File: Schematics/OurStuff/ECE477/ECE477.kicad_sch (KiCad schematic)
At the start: 50 parts, among them J1 USB_B_Micro, J2 Barrel_Jack, J3 OLED JST PH 7pin, J4 Microphone Connector, J5 Conn_01x02_Pin, J6 Conn_01x02_Pin, Q1 SS8050-G, Q2 SS8050-G, SW1 Boot Button, SW2 RST Button, SW3 Button 1, SW4 Button 2, U1 ESP32-WROOM-32E, U2 CP2102N-Axx-xQFN28, U3 D30V30F3

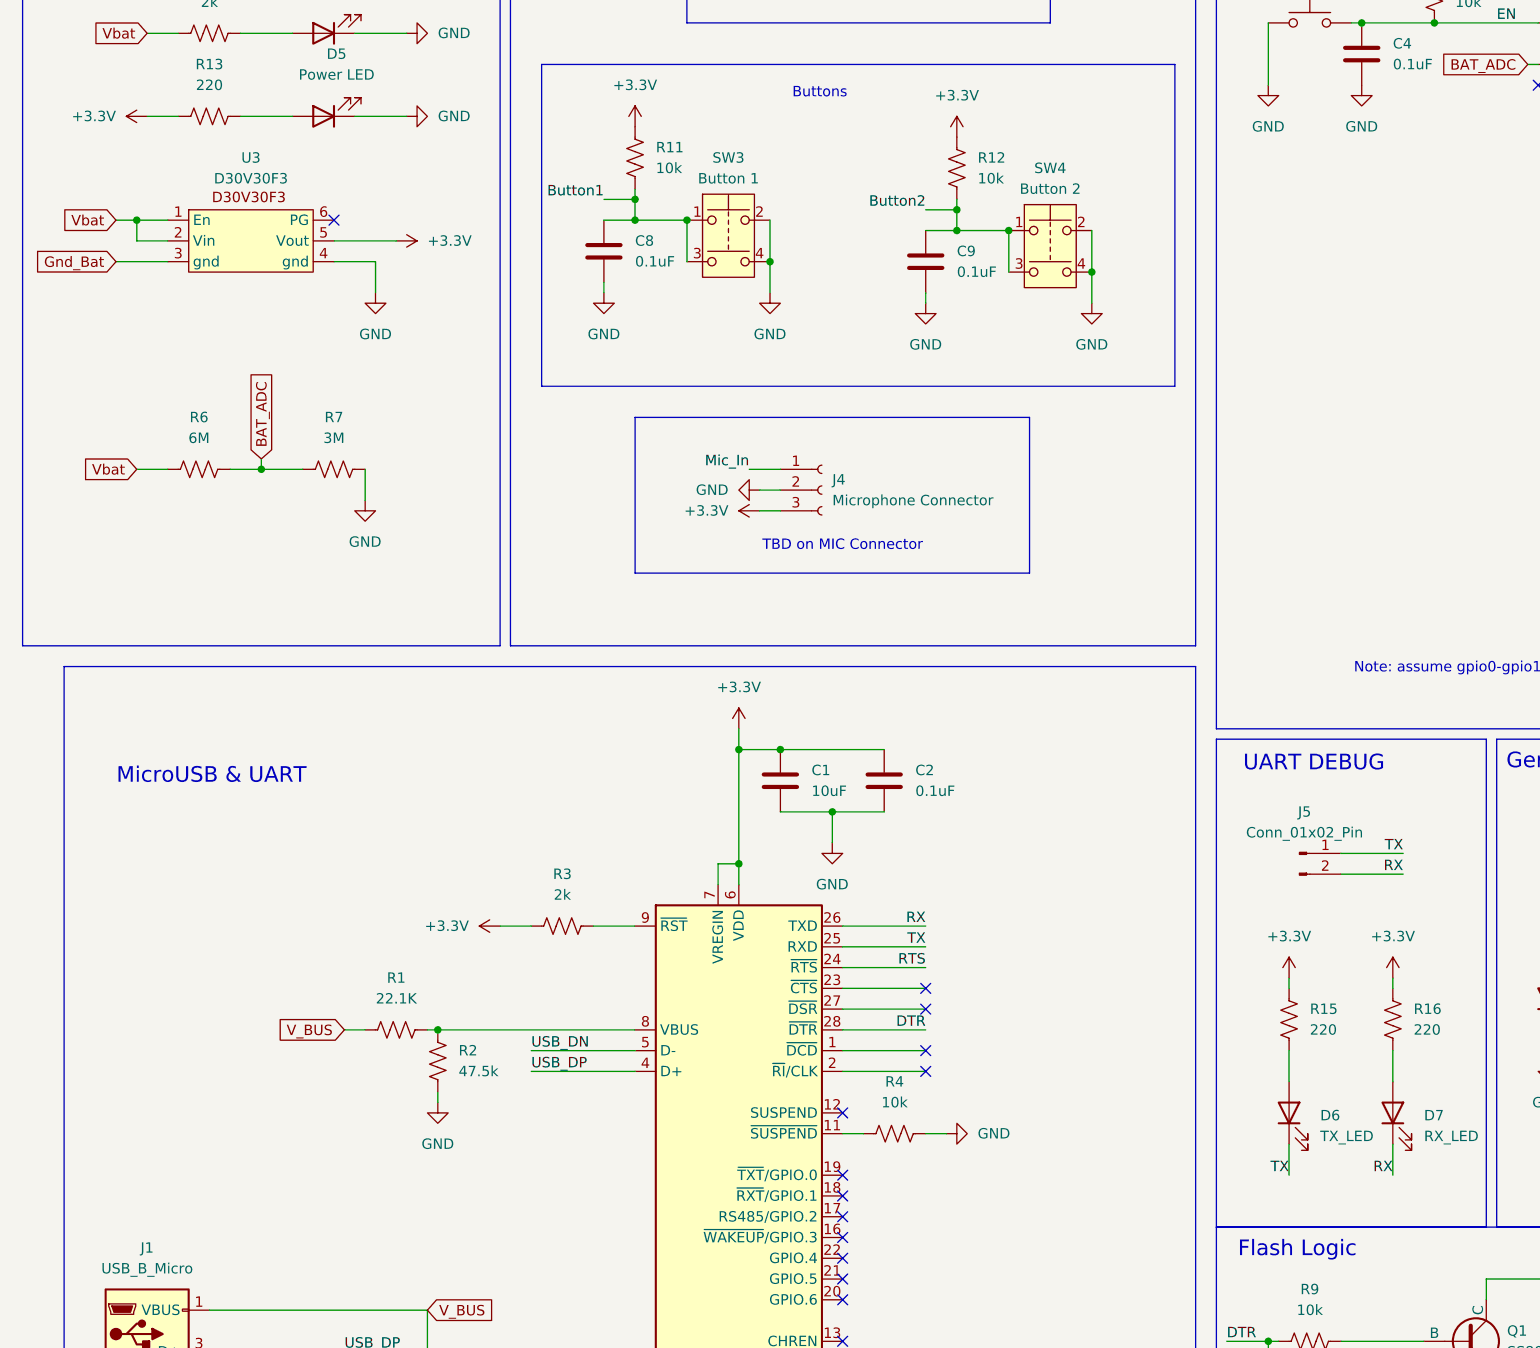
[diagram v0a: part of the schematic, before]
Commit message: fixed mistakes & almost finished footprints
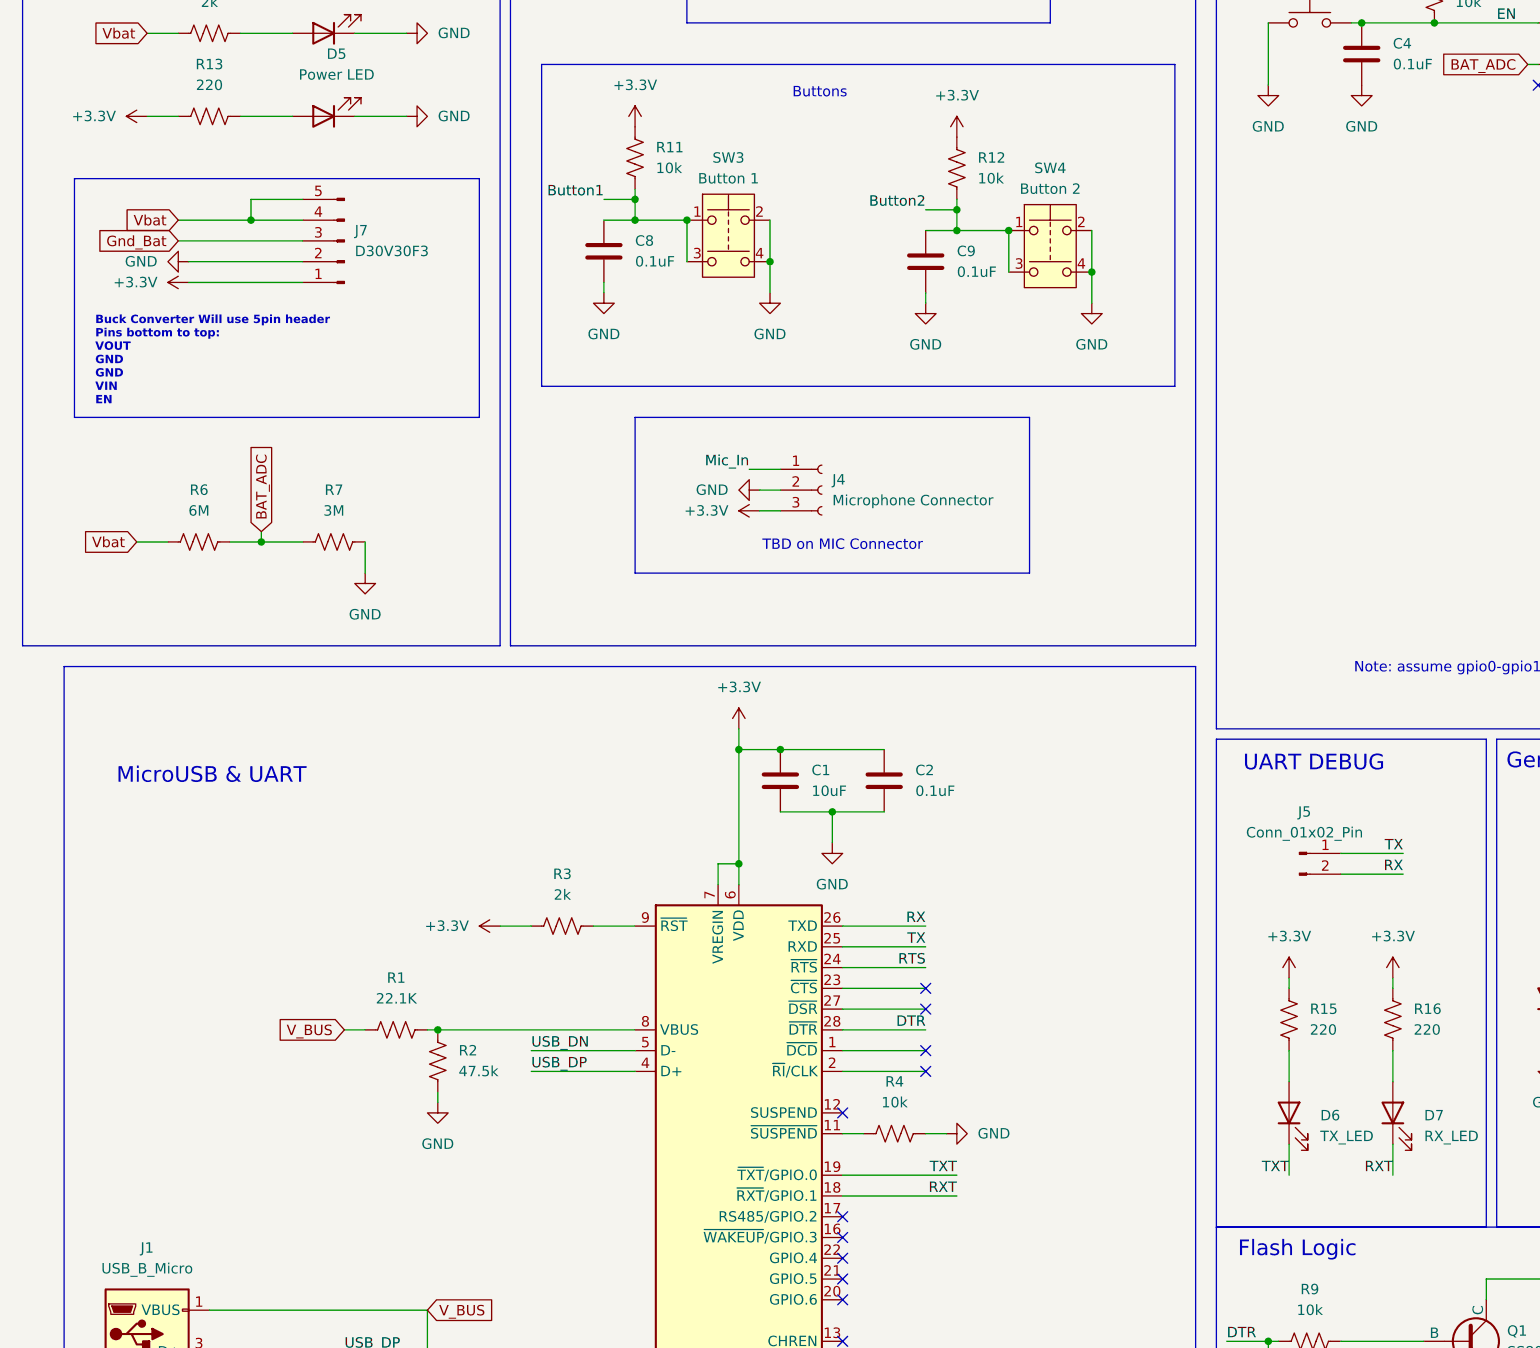
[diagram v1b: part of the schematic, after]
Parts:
- removed U3: D30V30F3, symbol D30V30F3:D30V30F3
- added J7: D30V30F3, Connector_PinHeader_2.54mm:PinHeader_1x05_P2.54mm_Vertical, symbol Connector:Conn_01x05_Pin
- J3: footprint (none) -> Connector_JST:JST_PH_B7B-PH-K_1x07_P2.00mm_Vertical
- J5, J6: footprint (none) -> Connector_PinHeader_2.54mm:PinHeader_1x02_P2.54mm_Vertical
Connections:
- net +3.3V: now also J7.1 (Pin_1)
- net GND: now also J7.2 (Pin_2)
- net Gnd_Bat: now also J7.3 (Pin_3)
- net RX: no longer D7.1 (K)
- net TX: no longer D6.1 (K)
- net Vbat: now also J7.4 (Pin_4), J7.5 (Pin_5)
- net RXT: now reaches U2.18 (~{RXT}/GPIO.1)
- net RXT: now also D7.1 (K)
- net TXT: now reaches U2.19 (~{TXT}/GPIO.0)
- net TXT: now also D6.1 (K)
- no-connect marks 30 -> 27
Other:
- note added: "Buck Converter Will use 5pin header Pins bottom to top: VOUT GND GND VIN EN"
- moved on the sheet: R6, R7

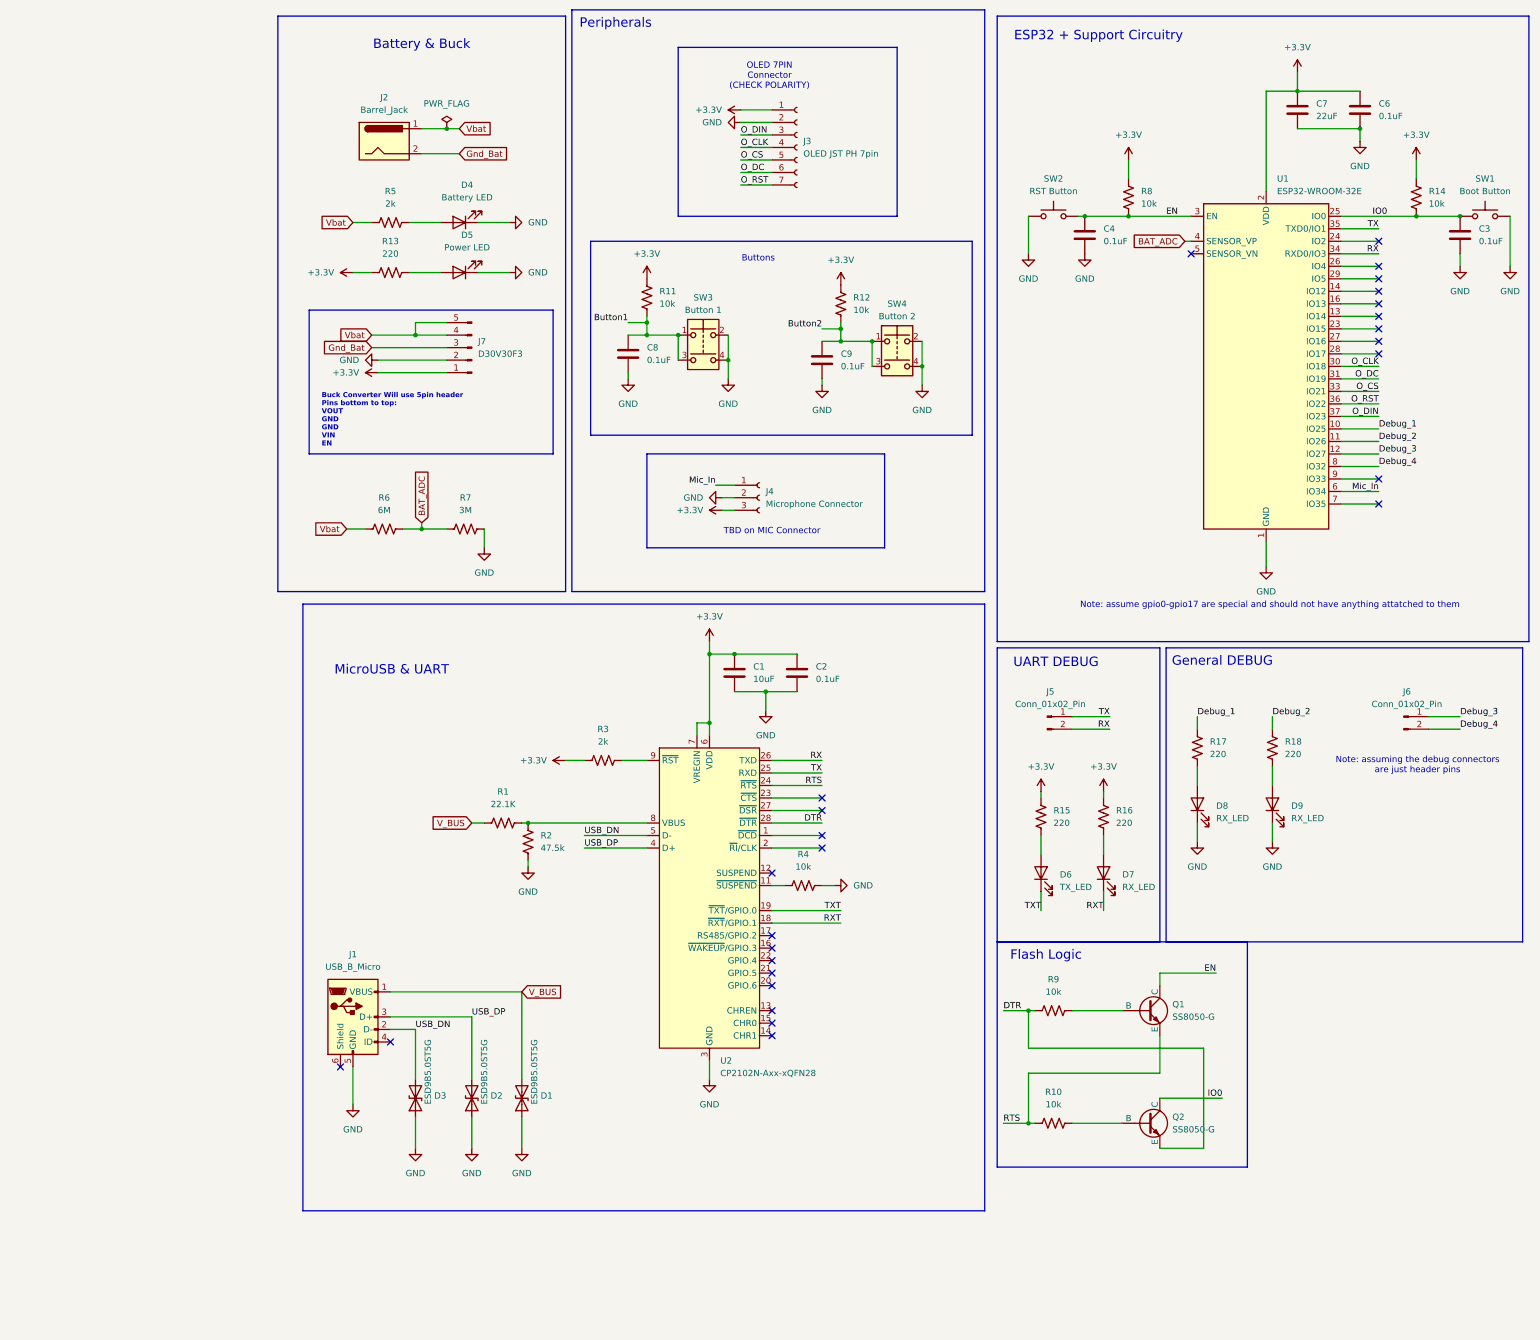
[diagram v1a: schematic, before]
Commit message: added test points and mounting holes
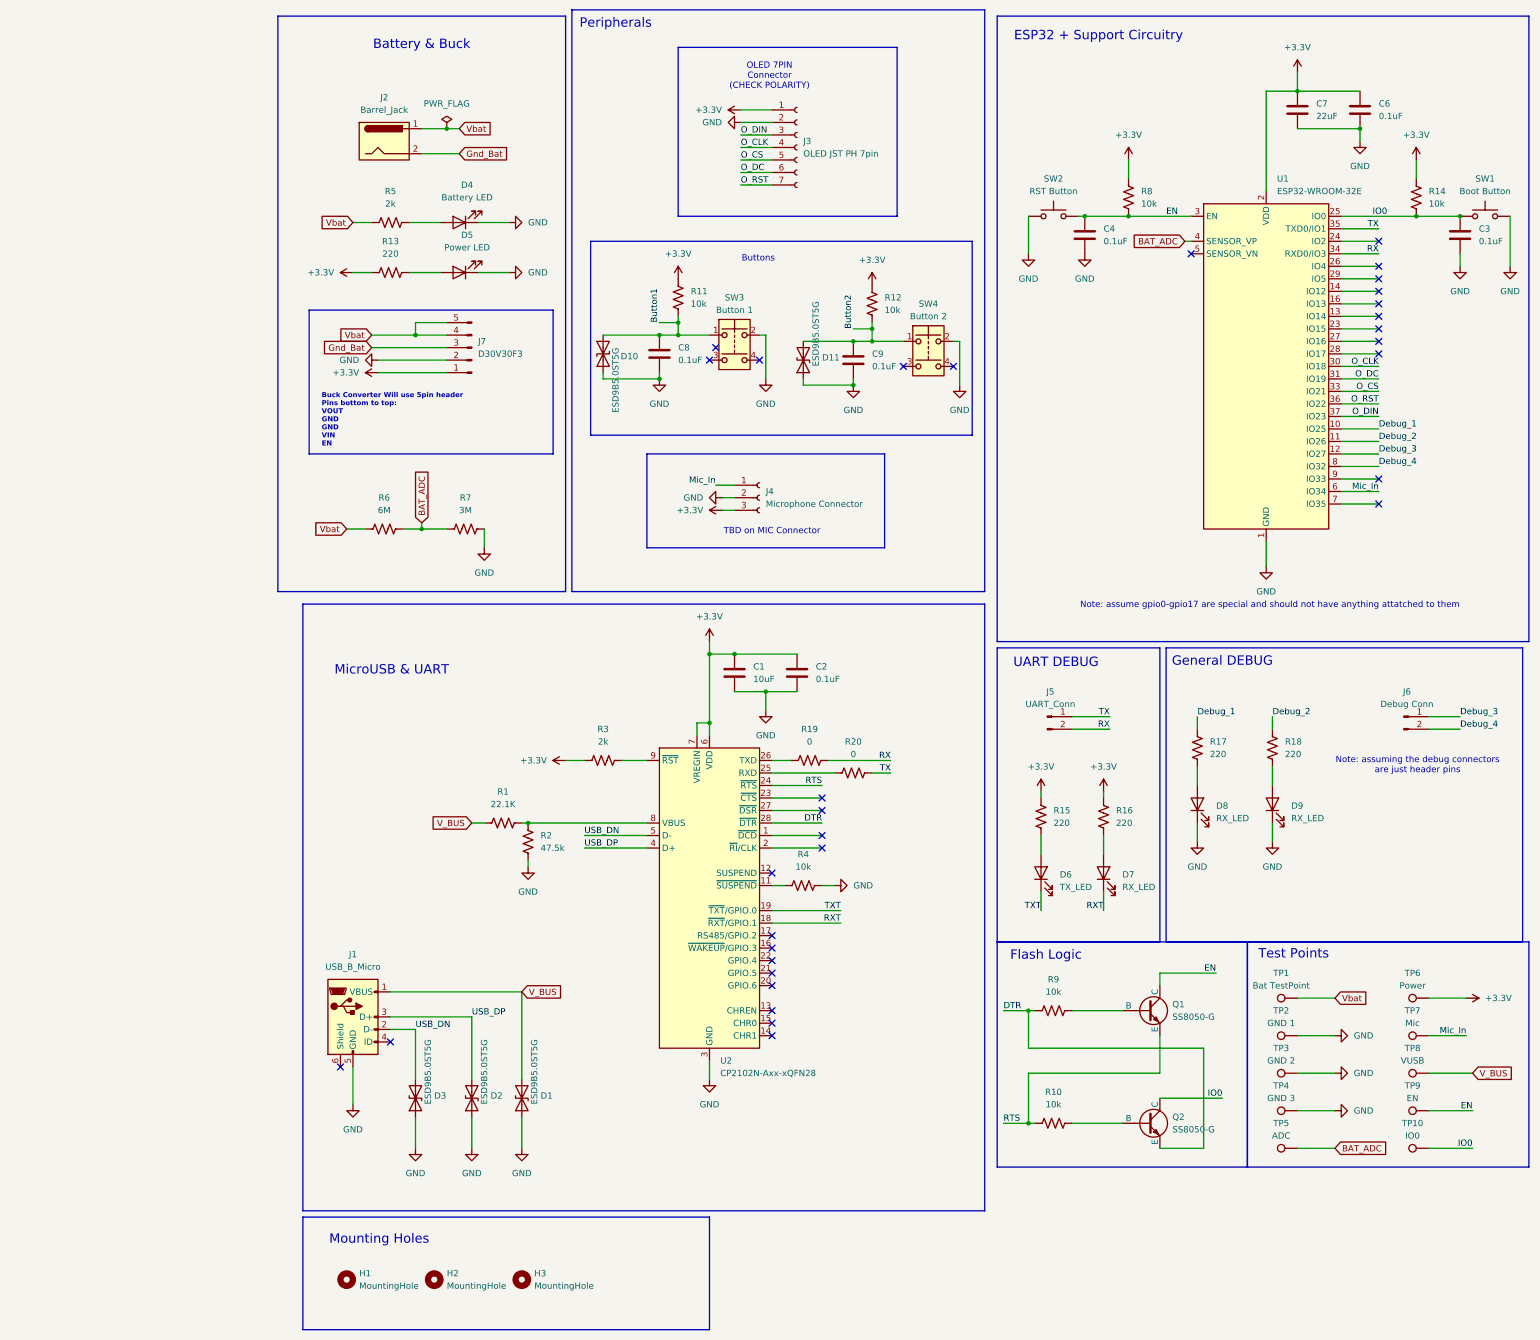
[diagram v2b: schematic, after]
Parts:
- added D10, D11: ESD9B5.0ST5G, Diode_SMD:D_SOD-923, symbol Device:D_TVS
- added H1, H2, H3: MountingHole, MountingHole:MountingHole_2.5mm, symbol Mechanical:MountingHole
- added R19, R20: 0, Resistor_SMD:R_0805_2012Metric_Pad1.20x1.40mm_HandSolder, symbol Device:R_US
- added TP1: Bat TestPoint, TestPoint:TestPoint_Keystone_5010-5014_Multipurpose, symbol Connector:TestPoint
- added TP10: IO0, TestPoint:TestPoint_Keystone_5010-5014_Multipurpose, symbol Connector:TestPoint
- added TP2: GND 1, TestPoint:TestPoint_Keystone_5010-5014_Multipurpose, symbol Connector:TestPoint
- added TP3: GND 2, TestPoint:TestPoint_Keystone_5010-5014_Multipurpose, symbol Connector:TestPoint
- added TP4: GND 3, TestPoint:TestPoint_Keystone_5010-5014_Multipurpose, symbol Connector:TestPoint
- added TP5: ADC, TestPoint:TestPoint_Keystone_5010-5014_Multipurpose, symbol Connector:TestPoint
- added TP6: Power, TestPoint:TestPoint_Keystone_5010-5014_Multipurpose, symbol Connector:TestPoint
- added TP7: Mic, TestPoint:TestPoint_Keystone_5010-5014_Multipurpose, symbol Connector:TestPoint
- added TP8: VUSB, TestPoint:TestPoint_Keystone_5010-5014_Multipurpose, symbol Connector:TestPoint
- added TP9: EN, TestPoint:TestPoint_Keystone_5010-5014_Multipurpose, symbol Connector:TestPoint
- D4, D5, D6, D7, D8, D9: footprint (none) -> LED_SMD:LED_0805_2012Metric_Pad1.15x1.40mm_HandSolder
- J1: footprint (none) -> Connector_USB:USB_Micro-B_Wuerth_614105150721_Vertical
- J2: footprint (none) -> Connector_BarrelJack:BarrelJack_Wuerth_6941xx301002
- J4: footprint (none) -> Connector_PinHeader_2.54mm:PinHeader_1x03_P2.54mm_Vertical
- J5: value Conn_01x02_Pin -> UART_Conn
- J6: value Conn_01x02_Pin -> Debug Conn
- SW1, SW2: footprint (none) -> Button_Switch_THT:SW_PUSH_1P1T_6x3.5mm_H4.3_APEM_MJTP1243
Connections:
- net +3.3V: now also TP6.1
- net BAT_ADC: now also TP5.1
- net Button1: now also D10.1 (A1); no longer SW3.3
- net Button2: now also D11.2 (A2); no longer SW4.3
- net EN: now also TP9.1
- net GND: now also D10.2 (A2), D11.1 (A1), TP2.1, TP3.1, TP4.1; no longer SW3.4, SW4.4
- net IO0: now also TP10.1
- net Mic_In: now also TP7.1
- net RX: now also R19.1; no longer U2.26 (TXD)
- net TX: now also R20.1; no longer U2.25 (RXD)
- net V_BUS: now also TP8.1
- net Vbat: now also TP1.1
- new net: R19.2, U2.26 (TXD)
- new net: R20.2, U2.25 (RXD)
- no-connect marks 27 -> 32
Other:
- note added: "Mounting Holes"
- note added: "Test Points"
- moved on the sheet: C8, C9, R11, R12, SW3, SW4
